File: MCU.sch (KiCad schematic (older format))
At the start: 19 parts, among them J6 SWO, U3 STM32F401RCTx, Y1 20Mhz

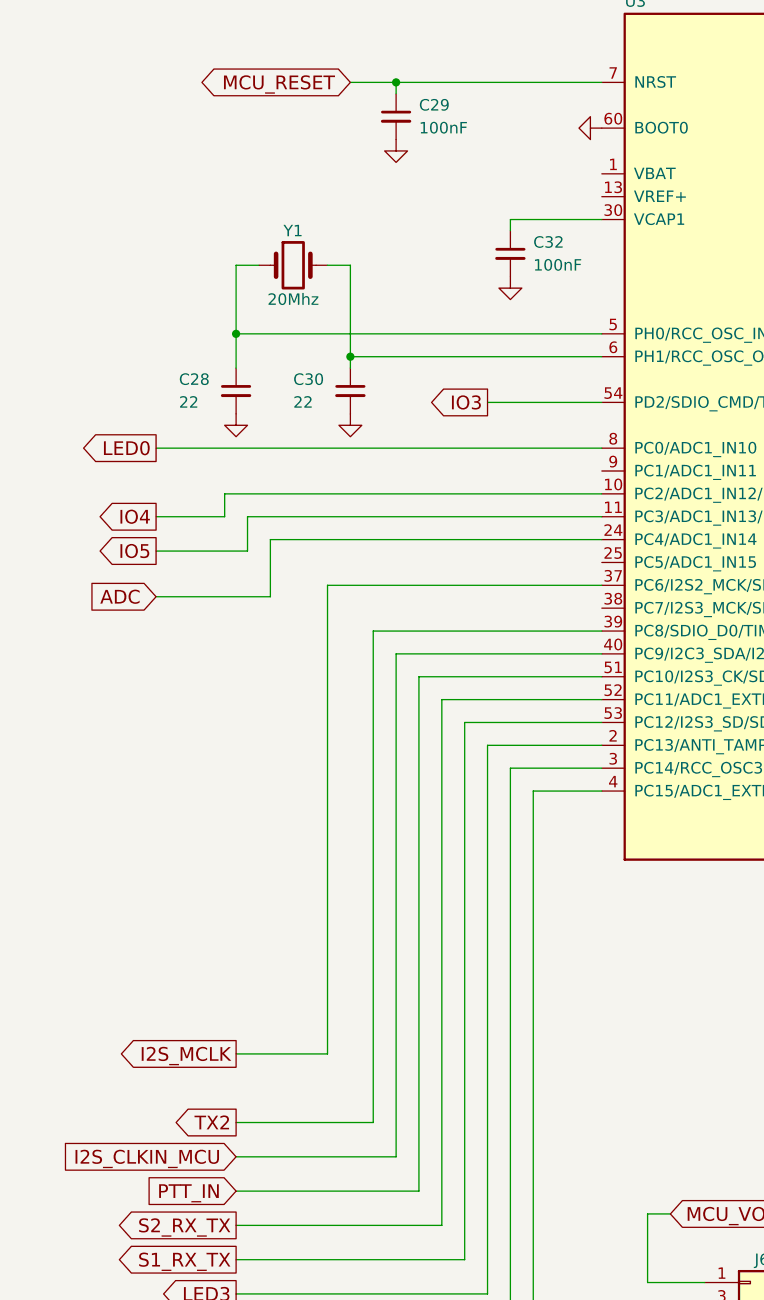
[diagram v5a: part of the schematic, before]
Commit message: PCB for 98.304Mhz generator
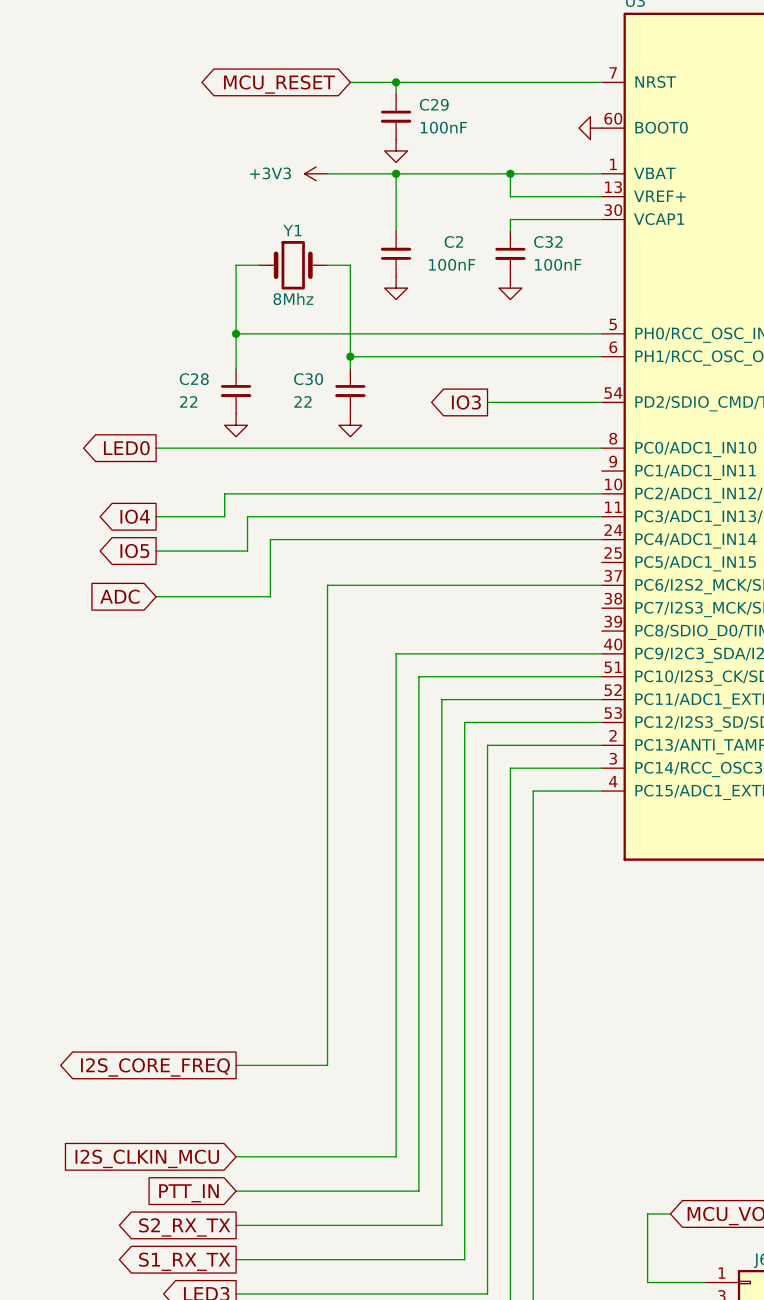
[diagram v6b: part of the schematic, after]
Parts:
- added C2: 100nF, UI:C_1206_0603, symbol C_Small
- U3: footprint Housings_QFP:LQFP-64_10x10mm_Pitch0.5mm -> Housings_QFP:TQFP-64_10x10mm_Pitch0.5mm
- Y1: value 20Mhz -> 8Mhz
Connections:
- net +3V3: now also U3.1 (VBAT), U3.13 (VREF+), C2.2
- net GND: now also C2.1
- net I2S_MCLK renamed I2S_CORE_FREQ
- net TX2: no longer names the net of U3.39 (PC8/SDIO_D0/TIM3_CH3/USART6_CK)
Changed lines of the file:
@@
 LIBS:cmos4000
 LIBS:conn
+LIBS:Oscillators
 LIBS:LCSDR-cache
 EELAYER 25 0
@@
 Comment4 ""
 $EndDescr
-Text GLabel 2050 6100 0    60   Output ~ 0
-I2S_MCLK
 Text GLabel 10000 5900 2    60   BiDi ~ 0
 I2S_SDO
@@
 SWO
 $Comp
-L GND #PWR042
+L GND #PWR044
 U 1 1 5DD650F1
 P 6150 5450
-F 0 "#PWR042" H 6150 5200 50  0001 C CNN
+F 0 "#PWR044" H 6150 5200 50  0001 C CNN
 F 1 "GND" H 6150 5300 50  0001 C CNN
 F 2 "" H 6150 5450 50  0001 C CNN
@@
 $EndComp
 $Comp
-L GND #PWR043
+L GND #PWR045
 U 1 1 5DD65332
 P 3250 2700
-F 0 "#PWR043" H 3250 2450 50  0001 C CNN
+F 0 "#PWR045" H 3250 2450 50  0001 C CNN
 F 1 "GND" H 3250 2550 50  0001 C CNN
 F 2 "" H 3250 2700 50  0001 C CNN
@@
 P 2300 2650
 F 0 "Y1" H 2300 2800 50  0000 C CNN
-F 1 "20Mhz" H 2300 2500 50  0000 C CNN
+F 1 "8Mhz" H 2300 2500 50  0000 C CNN
 F 2 "Crystals:Crystal_HC49-U_Vertical" H 2300 2650 50  0001 C CNN
 F 3 "" H 2300 2650 50  0001 C CNN
@@
 $EndComp
 $Comp
-L GND #PWR044
+L GND #PWR046
 U 1 1 5DD655DB
 P 2050 3300
-F 0 "#PWR044" H 2050 3050 50  0001 C CNN
+F 0 "#PWR046" H 2050 3050 50  0001 C CNN
 F 1 "GND" H 2050 3150 50  0001 C CNN
 F 2 "" H 2050 3300 50  0001 C CNN
@@
 $EndComp
 $Comp
-L GND #PWR045
+L GND #PWR047
 U 1 1 5DD65924
 P 2750 2100
-F 0 "#PWR045" H 2750 1850 50  0001 C CNN
+F 0 "#PWR047" H 2750 1850 50  0001 C CNN
 F 1 "GND" H 2750 1950 50  0001 C CNN
 F 2 "" H 2750 2100 50  0001 C CNN
@@
 $EndComp
 $Comp
-L +3V3 #PWR046
+L +3V3 #PWR048
 U 1 1 5DDA012B
 P 5550 1300
-F 0 "#PWR046" H 5550 1150 50  0001 C CNN
+F 0 "#PWR048" H 5550 1150 50  0001 C CNN
 F 1 "+3V3" V 5550 1550 50  0000 C CNN
 F 2 "" H 5550 1300 50  0001 C CNN
@@
 $EndComp
 $Comp
-L +3V3 #PWR047
+L +3V3 #PWR049
 U 1 1 5DDA0C93
 P 6600 650
-F 0 "#PWR047" H 6600 500 50  0001 C CNN
+F 0 "#PWR049" H 6600 500 50  0001 C CNN
 F 1 "+3V3" V 6600 900 50  0000 C CNN
 F 2 "" H 6600 650 50  0001 C CNN
@@
 $EndComp
 $Comp
-L GND #PWR048
+L GND #PWR050
 U 1 1 5DDA0E68
 P 6800 900
-F 0 "#PWR048" H 6800 650 50  0001 C CNN
+F 0 "#PWR050" H 6800 650 50  0001 C CNN
 F 1 "GND" H 6800 750 50  0001 C CNN
 F 2 "" H 6800 900 50  0001 C CNN
@@
 $EndComp
 $Comp
-L GND #PWR049
+L GND #PWR051
 U 1 1 5DDA0EDC
 P 7300 900
-F 0 "#PWR049" H 7300 650 50  0001 C CNN
+F 0 "#PWR051" H 7300 650 50  0001 C CNN
 F 1 "GND" H 7300 750 50  0001 C CNN
 F 2 "" H 7300 900 50  0001 C CNN
@@
 $EndComp
 $Comp
-L GND #PWR050
+L GND #PWR052
 U 1 1 5DDA0F4B
 P 7800 900
-F 0 "#PWR050" H 7800 650 50  0001 C CNN
+F 0 "#PWR052" H 7800 650 50  0001 C CNN
 F 1 "GND" H 7800 750 50  0001 C CNN
 F 2 "" H 7800 900 50  0001 C CNN
@@
 Text GLabel 1700 3900 0    60   Output ~ 0
 IO5
-Text GLabel 2050 6400 0    60   Output ~ 0
-TX2
-$Comp
-L GND #PWR051
+Text GLabel 2050 6150 0    60   Output ~ 0
+I2S_CORE_FREQ
+$Comp
+L GND #PWR053
 U 1 1 5DDFAF2B
 P 3650 2050
-F 0 "#PWR051" H 3650 1800 50  0001 C CNN
+F 0 "#PWR053" H 3650 1800 50  0001 C CNN
 F 1 "GND" H 3650 1900 50  0001 C CNN
 F 2 "" H 3650 2050 50  0001 C CNN
@@
 F 0 "U3" H 3750 5375 50  0000 L BNN
 F 1 "STM32F401RCTx" H 8150 5375 50  0000 R BNN
-F 2 "Housings_QFP:LQFP-64_10x10mm_Pitch0.5mm" H 8150 5325 50  0001 R TNN
+F 2 "Housings_QFP:TQFP-64_10x10mm_Pitch0.5mm" H 8150 5325 50  0001 R TNN
 F 3 "" H 5950 3450 50  0001 C CNN
 	1    5950 3450
@@
 Text GLabel 10000 600  2    60   Output ~ 0
 BAND
-Wire Wire Line
-	2450 4050 3650 4050
 Wire Wire Line
 	8300 5900 10000 5900
@@
 	9400 3850 8250 3850
 Wire Wire Line
-	2050 6100 2450 6100
-Wire Wire Line
-	2450 6100 2450 4050
-Wire Wire Line
 	8700 4550 8250 4550
 Wire Wire Line
@@
 Wire Wire Line
 	8700 5250 8700 4550
-Wire Wire Line
-	2050 6400 2650 6400
-Wire Wire Line
-	2650 6400 2650 4250
-Wire Wire Line
-	2650 4250 3650 4250
-$Comp
-L GND #PWR052
+$Comp
+L GND #PWR054
 U 1 1 5DD65598
 P 2550 3300
-F 0 "#PWR052" H 2550 3050 50  0001 C CNN
+F 0 "#PWR054" H 2550 3050 50  0001 C CNN
 F 1 "GND" H 2550 3150 50  0001 C CNN
 F 2 "" H 2550 3300 50  0001 C CNN
@@
 	5800 7550 6150 7550
 $Comp
-L GND #PWR053
+L GND #PWR055
 U 1 1 5EAA5CF7
 P 3850 7550
-F 0 "#PWR053" H 3850 7300 50  0001 C CNN
+F 0 "#PWR055" H 3850 7300 50  0001 C CNN
 F 1 "GND" H 3850 7400 50  0001 C CNN
 F 2 "" H 3850 7550 50  0001 C CNN
@@
 $EndComp
 $Comp
-L GND #PWR054
+L GND #PWR056
 U 1 1 5EAAAE5C
 P 4600 6150
-F 0 "#PWR054" H 4600 5900 50  0001 C CNN
+F 0 "#PWR056" H 4600 5900 50  0001 C CNN
 F 1 "GND" H 4600 6000 50  0001 C CNN
 F 2 "" H 4600 6150 50  0001 C CNN
@@
 	7300 5600 7400 5600
 $Comp
-L GND #PWR055
+L GND #PWR057
 U 1 1 5EBB9402
 P 6950 5600
-F 0 "#PWR055" H 6950 5350 50  0001 C CNN
+F 0 "#PWR057" H 6950 5350 50  0001 C CNN
 F 1 "GND" H 6950 5450 50  0001 C CNN
 F 2 "" H 6950 5600 50  0001 C CNN
@@
 $EndComp
 $Comp
-L GND #PWR056
+L GND #PWR058
 U 1 1 5EBB9D8B
 P 6950 6050
-F 0 "#PWR056" H 6950 5800 50  0001 C CNN
+F 0 "#PWR058" H 6950 5800 50  0001 C CNN
 F 1 "GND" H 6950 5900 50  0001 C CNN
 F 2 "" H 6950 6050 50  0001 C CNN
@@
 	7600 6050 7750 6050
 $Comp
-L GND #PWR057
+L GND #PWR059
 U 1 1 5EBBA1A1
 P 4600 5800
-F 0 "#PWR057" H 4600 5550 50  0001 C CNN
+F 0 "#PWR059" H 4600 5550 50  0001 C CNN
 F 1 "GND" H 4600 5650 50  0001 C CNN
 F 2 "" H 4600 5800 50  0001 C CNN
@@
 Wire Wire Line
 	8900 4350 8250 4350
+Wire Wire Line
+	3650 2350 3250 2350
+Wire Wire Line
+	3250 2350 3250 2250
+Wire Wire Line
+	2450 2250 3650 2250
+$Comp
+L +3V3 #PWR060
+U 1 1 5EE9C3CD
+P 2450 2250
+F 0 "#PWR060" H 2450 2100 50  0001 C CNN
+F 1 "+3V3" V 2450 2500 50  0000 C CNN
+F 2 "" H 2450 2250 50  0001 C CNN
+F 3 "" H 2450 2250 50  0001 C CNN
+	1    2450 2250
+	0    -1   -1   0
+$EndComp
+$Comp
+L C_Small C2
+U 1 1 5EE9C470
+P 2750 2600
+F 0 "C2" H 2450 2550 50  0000 L CNN
+F 1 "100nF" H 2400 2650 50  0000 L CNN
+F 2 "UI:C_1206_0603" H 2750 2600 50  0001 C CNN
+F 3 "" H 2750 2600 50  0001 C CNN
+	1    2750 2600
+	-1   0    0    1
+$EndComp
+$Comp
+L GND #PWR061
+U 1 1 5EE9C566
+P 2750 2700
+F 0 "#PWR061" H 2750 2450 50  0001 C CNN
+F 1 "GND" H 2750 2550 50  0001 C CNN
+F 2 "" H 2750 2700 50  0001 C CNN
+F 3 "" H 2750 2700 50  0001 C CNN
+	1    2750 2700
+	1    0    0    -1
+$EndComp
+Wire Wire Line
+	2750 2500 2750 2250
+Connection ~ 3250 2250
+Connection ~ 2750 2250
+Wire Wire Line
+	3650 4050 2450 4050
+Wire Wire Line
+	2450 4050 2450 6150
+Wire Wire Line
+	2450 6150 2050 6150
 $EndSCHEMATC
